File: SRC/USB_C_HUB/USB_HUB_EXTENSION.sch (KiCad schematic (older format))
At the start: 7 parts, among them IC1 TUSB2046BIRHBT, Y2 6MHz

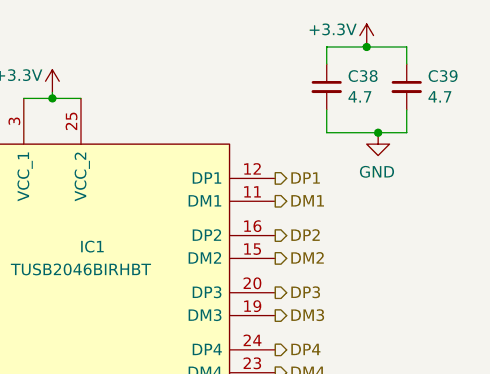
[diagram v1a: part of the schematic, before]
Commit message: schematic capture and footprint assignment complete. Pending approval
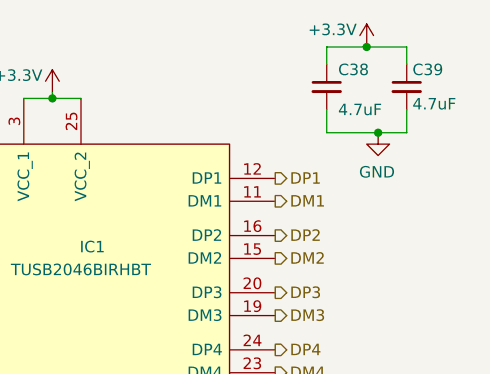
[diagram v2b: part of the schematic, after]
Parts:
- C36, C37: footprint (none) -> Capacitor_SMD:C_0402_1005Metric
- C38, C39: value 4.7 -> 4.7uF; footprint (none) -> Capacitor_SMD:C_0603_1608Metric; Mfr No. (none) -> CL10A475KQ8NNNC
- R14: footprint (none) -> Resistor_SMD:R_0402_1005Metric; Mfr No. (none) -> 49880500
- Y2: footprint (none) -> Crystal:Crystal_SMD_HC49-SD
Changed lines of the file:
@@
 AR Path="/660C6EC5" Ref="C?"  Part="1"
 AR Path="/6609E24E/660C6EC5" Ref="C38"  Part="1"
-F 0 "C38" H 5717 1071 50  0000 L CNN
-F 1 "4.7" H 5717 980 50  0000 L CNN
-F 2 "" H 5625 1025 50  0001 C CNN
+F 0 "C38" H 5675 1100 50  0000 L CNN
+F 1 "4.7uF" H 5675 925 50  0000 L CNN
+F 2 "Capacitor_SMD:C_0603_1608Metric" H 5625 1025 50  0001 C CNN
 F 3 "~" H 5625 1025 50  0001 C CNN
+F 4 "CL10A475KQ8NNNC" H 5625 1025 50  0001 C CNN "Mfr No."
 	1    5625 1025
 	1    0    0    -1
@@
 AR Path="/660D9F3B" Ref="C?"  Part="1"
 AR Path="/6609E24E/660D9F3B" Ref="C39"  Part="1"
-F 0 "C39" H 6067 1071 50  0000 L CNN
-F 1 "4.7" H 6067 980 50  0000 L CNN
-F 2 "" H 5975 1025 50  0001 C CNN
+F 0 "C39" H 6000 1100 50  0000 L CNN
+F 1 "4.7uF" H 6000 950 50  0000 L CNN
+F 2 "Capacitor_SMD:C_0603_1608Metric" H 5975 1025 50  0001 C CNN
 F 3 "~" H 5975 1025 50  0001 C CNN
+F 4 "CL10A475KQ8NNNC" H 5975 1025 50  0001 C CNN "Mfr No."
 	1    5975 1025
 	1    0    0    -1
@@
 F 0 "Y2" V 1979 2356 50  0000 L CNN
 F 1 "6MHz" V 2070 2356 50  0000 L CNN
-F 2 "" H 2025 2225 50  0001 C CNN
+F 2 "Crystal:Crystal_SMD_HC49-SD" H 2025 2225 50  0001 C CNN
 F 3 "~" H 2025 2225 50  0001 C CNN
 F 4 "AS-6.000-12-2020-EXT-SMD-TR" V 2025 2225 50  0001 C CNN "Mfr No."
@@
 F 0 "C37" V 1371 1925 50  0000 C CNN
 F 1 "22pF" V 1462 1925 50  0000 C CNN
-F 2 "" H 1600 1925 50  0001 C CNN
+F 2 "Capacitor_SMD:C_0402_1005Metric" H 1600 1925 50  0001 C CNN
 F 3 "~" H 1600 1925 50  0001 C CNN
 	1    1600 1925
@@
 F 0 "C36" V 1346 2475 50  0000 C CNN
 F 1 "22pF" V 1437 2475 50  0000 C CNN
-F 2 "" H 1575 2475 50  0001 C CNN
+F 2 "Capacitor_SMD:C_0402_1005Metric" H 1575 2475 50  0001 C CNN
 F 3 "~" H 1575 2475 50  0001 C CNN
 	1    1575 2475
@@
 F 0 "R14" H 3293 1296 50  0000 L CNN
 F 1 "10K" H 3293 1205 50  0000 L CNN
-F 2 "" V 3265 1240 50  0001 C CNN
+F 2 "Resistor_SMD:R_0402_1005Metric" V 3265 1240 50  0001 C CNN
 F 3 "~" H 3225 1250 50  0001 C CNN
+F 4 "49880500 " H 3225 1250 50  0001 C CNN "Mfr No."
 	1    3225 1250
 	1    0    0    -1
